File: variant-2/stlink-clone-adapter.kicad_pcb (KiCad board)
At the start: 2 copper layers, 15 x 14.2 mm, 2 parts, among them J1 2X5_HDR, J2 ARM_10PIN

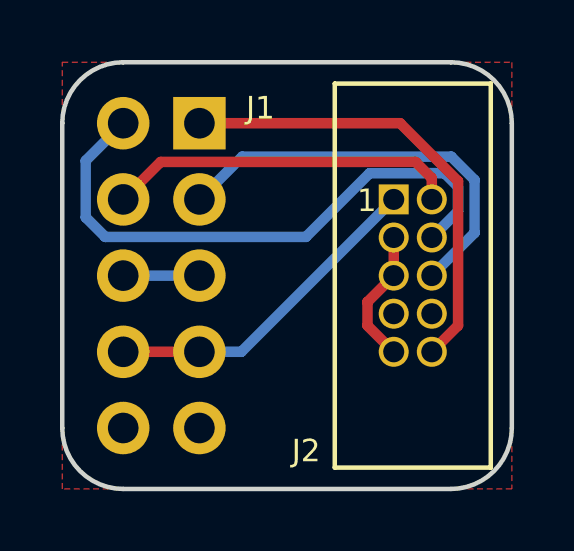
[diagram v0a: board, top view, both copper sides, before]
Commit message: pour bottom ground
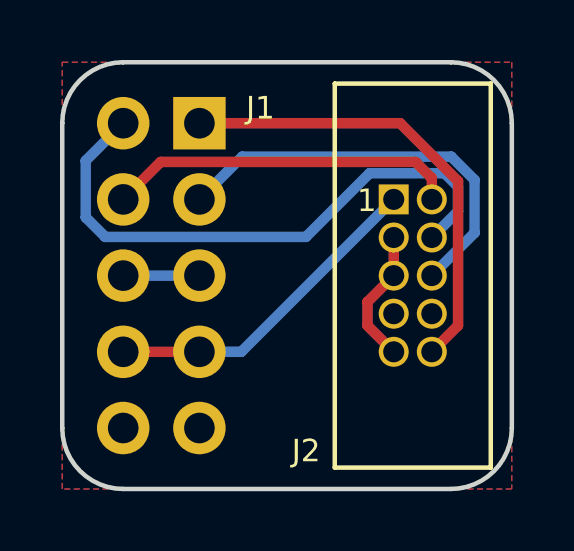
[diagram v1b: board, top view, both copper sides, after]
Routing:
- added copper zone on B.Cu, net /GND
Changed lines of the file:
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@@
-(kicad_pcb (version 20171130) (host pcbnew 5.1.8-db9833491~88~ubuntu20.04.1)
+(kicad_pcb (version 20171130) (host pcbnew 5.1.9-73d0e3b20d~88~ubuntu20.10.1)
   (general
     (thickness 1.6)
@@
   )
   (setup
-    (last_trace_width 0.35)
+    (last_trace_width 0.25)
     (user_trace_width 0.35)
     (trace_clearance 0.2)
@@
       (effects (font (size 0.75 0.75) (thickness 0.12)))
     )
+    (fp_line (start 2.6 -6.4) (end 2.6 6.4) (layer F.SilkS) (width 0.15))
+    (fp_line (start 2.6 6.4) (end -2.6 6.4) (layer F.SilkS) (width 0.15))
+    (fp_line (start -2.6 6.4) (end -2.6 -6.4) (layer F.SilkS) (width 0.15))
     (fp_line (start -2.6 -6.4) (end 2.6 -6.4) (layer F.SilkS) (width 0.15))
-    (fp_line (start -2.6 6.4) (end -2.6 -6.4) (layer F.SilkS) (width 0.15))
-    (fp_line (start 2.6 6.4) (end -2.6 6.4) (layer F.SilkS) (width 0.15))
-    (fp_line (start 2.6 -6.4) (end 2.6 6.4) (layer F.SilkS) (width 0.15))
     (fp_text user 1 (at -1.535 -2.5) (layer F.SilkS)
       (effects (font (size 0.75 0.75) (thickness 0.12)))
@@
   (segment (start 151.765 112.776) (end 156.845 107.696) (width 0.35) (layer B.Cu) (net 6) (status 20))
   (segment (start 147.828 112.776) (end 150.368 112.776) (width 0.35) (layer F.Cu) (net 6) (status 30))
+  (zone (net 3) (net_name /GND) (layer B.Cu) (hatch edge 0.508)
+    (connect_pads (clearance 0.35))
+    (min_thickness 0.254)
+    (fill yes (arc_segments 16) (thermal_gap 0.35) (thermal_bridge_width 0.35))
+    (polygon
+      (pts
+        (xy 160.782 117.348) (xy 145.796 117.348) (xy 145.796 103.124) (xy 160.782 103.124)
+      )
+    )
+  )
   (zone (net 3) (net_name /GND) (layer F.Cu) (hatch edge 0.508)
     (connect_pads (clearance 0.35))
